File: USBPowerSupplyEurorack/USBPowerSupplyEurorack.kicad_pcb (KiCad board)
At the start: 2 copper layers, 9.8 x 110 mm, 21 parts, among them J1 1734366-1, J2 95278-501A10LF, Q1 Q_PMOS_GSD

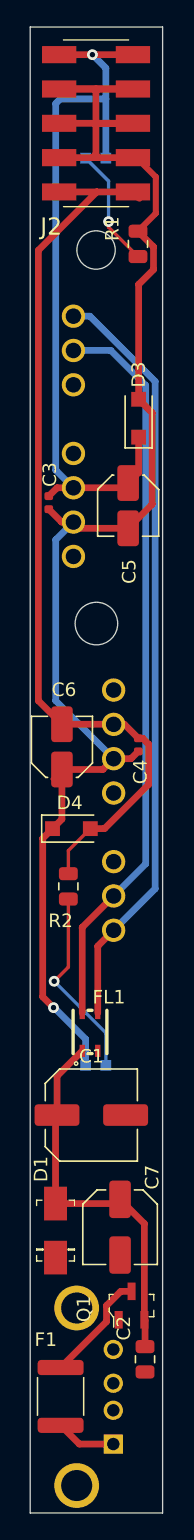
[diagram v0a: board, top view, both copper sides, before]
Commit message: going to 4hp for better routing
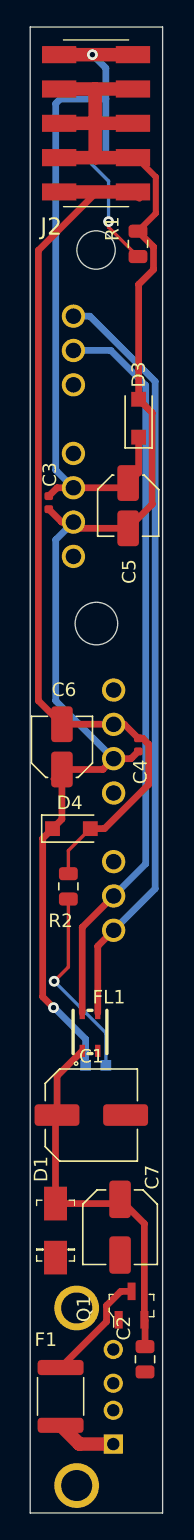
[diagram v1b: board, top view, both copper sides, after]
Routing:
- net 0V: track 118.4 -> 128.9 mm
- net -12V: track 67.7 -> 73.2 mm
- net +12V: track 56.4 -> 61.8 mm
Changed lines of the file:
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@@
     (thickness 1.6)
     (drawings 6)
-    (tracks 118)
+    (tracks 125)
     (zones 0)
     (modules 21)
@@
   )
   (setup
-    (last_trace_width 0.25)
+    (last_trace_width 1)
     (user_trace_width 0.2)
     (user_trace_width 0.25)
@@
     (user_trace_width 0.45)
     (user_trace_width 0.5)
+    (user_trace_width 1)
+    (user_trace_width 2)
     (trace_clearance 0.2)
     (zone_clearance 0.508)
@@
   (gr_line (start 144.35 158.1) (end 134.55 158.1) (layer Edge.Cuts) (width 0.001))
   (gr_line (start 144.35 48.125) (end 144.35 158.1) (layer Edge.Cuts) (width 0.001))
+  (segment (start 136.5375 125.7625) (end 138.4 123.9) (width 0.5) (layer F.Cu) (net 1))
+  (segment (start 136.5375 128.65) (end 136.5375 125.7625) (width 0.5) (layer F.Cu) (net 1))
+  (segment (start 143.05 145.7875) (end 143.05 143.85) (width 0.5) (layer F.Cu) (net 1))
   (segment (start 143.05 143.85) (end 143 143.8) (width 0.5) (layer F.Cu) (net 1))
-  (segment (start 143.05 145.7875) (end 143.05 143.85) (width 0.5) (layer F.Cu) (net 1))
   (segment (start 143 136.6875) (end 141.2 134.8875) (width 0.5) (layer F.Cu) (net 1))
   (segment (start 143 143.8) (end 143 136.6875) (width 0.5) (layer F.Cu) (net 1))
@@
   (segment (start 136.425 128.7625) (end 136.5375 128.65) (width 0.5) (layer F.Cu) (net 1))
   (segment (start 136.425 135.2) (end 136.425 128.7625) (width 0.5) (layer F.Cu) (net 1))
-  (segment (start 136.5375 125.7625) (end 138.4 123.9) (width 0.5) (layer F.Cu) (net 1))
-  (segment (start 136.5375 128.65) (end 136.5375 125.7625) (width 0.5) (layer F.Cu) (net 1))
+  (segment (start 141.25 141.7) (end 142.05 141.7) (width 0.5) (layer F.Cu) (net 2))
+  (segment (start 140.2 143.9375) (end 140.2 142.75) (width 0.5) (layer F.Cu) (net 2))
   (segment (start 136.8 147.3375) (end 140.2 143.9375) (width 0.5) (layer F.Cu) (net 2))
-  (segment (start 141.25 141.7) (end 142.05 141.7) (width 0.5) (layer F.Cu) (net 2))
   (segment (start 140.2 142.75) (end 141.25 141.7) (width 0.5) (layer F.Cu) (net 2))
-  (segment (start 140.2 143.9375) (end 140.2 142.75) (width 0.5) (layer F.Cu) (net 2))
   (segment (start 136.2125 107.4625) (end 136.2 107.45) (width 0.5) (layer F.Cu) (net 3))
   (segment (start 136.2 103.775) (end 136.9 103.075) (width 0.3) (layer F.Cu) (net 3))
@@
   (segment (start 136.437499 86.077501) (end 136.437499 97.987499) (width 0.5) (layer B.Cu) (net 3))
   (segment (start 137.75 84.765) (end 136.437499 86.077501) (width 0.5) (layer B.Cu) (net 3))
-  (segment (start 136.695 55.25) (end 142.155 55.25) (width 0.5) (layer F.Cu) (net 3))
   (segment (start 139.415 57.535) (end 139.16 57.79) (width 0.5) (layer F.Cu) (net 3))
   (segment (start 139.16 57.79) (end 142.155 57.79) (width 0.5) (layer F.Cu) (net 3))
@@
   (segment (start 138.21 85.225) (end 137.75 84.765) (width 0.5) (layer F.Cu) (net 3))
   (segment (start 141.8 85.225) (end 138.21 85.225) (width 0.5) (layer F.Cu) (net 3))
-  (segment (start 142.155 52.71) (end 136.695 52.71) (width 0.5) (layer F.Cu) (net 3))
   (segment (start 142.155 55.25) (end 139.45 55.25) (width 0.5) (layer F.Cu) (net 3))
   (segment (start 139.415 55.285) (end 139.415 57.535) (width 0.5) (layer F.Cu) (net 3))
   (segment (start 139.45 55.25) (end 139.415 55.285) (width 0.5) (layer F.Cu) (net 3))
   (segment (start 139.415 52.71) (end 139.415 55.285) (width 0.5) (layer F.Cu) (net 3))
+  (segment (start 136.695 55.25) (end 142.155 55.25) (width 1) (layer F.Cu) (net 3))
+  (segment (start 139.36 57.735) (end 139.415 57.79) (width 1) (layer F.Cu) (net 3))
+  (segment (start 139.36 52.71) (end 139.36 57.735) (width 1) (layer F.Cu) (net 3))
+  (segment (start 139.415 57.79) (end 142.155 57.79) (width 1) (layer F.Cu) (net 3))
+  (segment (start 136.695 57.79) (end 139.415 57.79) (width 1) (layer F.Cu) (net 3))
+  (segment (start 136.695 52.71) (end 139.36 52.71) (width 1) (layer F.Cu) (net 3))
+  (segment (start 139.36 52.71) (end 142.155 52.71) (width 1) (layer F.Cu) (net 3))
   (segment (start 141.52 99.735) (end 142.55 100.765) (width 0.5) (layer F.Cu) (net 4))
   (segment (start 140.725 99.735) (end 141.52 99.735) (width 0.5) (layer F.Cu) (net 4))
@@
   (segment (start 135.15499 64.65501) (end 135.15499 97.97999) (width 0.5) (layer F.Cu) (net 4))
   (segment (start 139.48 60.33) (end 142.155 60.33) (width 0.5) (layer F.Cu) (net 4))
+  (segment (start 136.695 60.33) (end 142.155 60.33) (width 1) (layer F.Cu) (net 4))
   (segment (start 142.575 81.1) (end 141.8 81.875) (width 0.5) (layer F.Cu) (net 5))
   (segment (start 142.575 78.475) (end 142.575 81.1) (width 0.5) (layer F.Cu) (net 5))
@@
   (segment (start 141.45 82.225) (end 141.8 81.875) (width 0.5) (layer F.Cu) (net 5))
   (segment (start 137.75 82.225) (end 141.45 82.225) (width 0.5) (layer F.Cu) (net 5))
-  (segment (start 138.1875 153) (end 136.8 151.6125) (width 0.5) (layer F.Cu) (net 6))
-  (segment (start 140.7 153) (end 138.1875 153) (width 0.5) (layer F.Cu) (net 6))
+  (segment (start 136.695 50.17) (end 142.155 50.17) (width 1) (layer F.Cu) (net 5))
+  (segment (start 140.7 153) (end 138.1875 153) (width 1) (layer F.Cu) (net 6))
+  (segment (start 138.1875 153) (end 136.8 151.6125) (width 1) (layer F.Cu) (net 6))
   (segment (start 138.4 114.76) (end 138.4 121.1) (width 0.5) (layer F.Cu) (net 9))
   (segment (start 140.725 112.435) (end 138.4 114.76) (width 0.5) (layer F.Cu) (net 9))
